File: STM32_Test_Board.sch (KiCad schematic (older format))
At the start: 7 parts, among them J1 Conn_01x16_Male, J2 Conn_01x16_Male, J3 Conn_01x16_Male, J4 Conn_01x16_Male, U1 STM32G484RET6

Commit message: Adding PCB design
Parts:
- U1: footprint LQFP64-10x10mm -> Package_QFP:LQFP-64_10x10mm_P0.5mm
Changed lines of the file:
@@
 F 0 "U1" H 5050 2537 60  0000 C CNN
 F 1 "STM32G484RET6" H 5050 2431 60  0000 C CNN
-F 2 "LQFP64-10x10mm" H 5050 2390 60  0001 C CNN
+F 2 "Package_QFP:LQFP-64_10x10mm_P0.5mm" H 5050 2390 60  0001 C CNN
 F 3 "" H 3650 2150 60  0000 C CNN
 	1    3650 2150
@@
 F 0 "U1" H 9650 3737 60  0000 C CNN
 F 1 "STM32G484RET6" H 9650 3631 60  0000 C CNN
-F 2 "LQFP64-10x10mm" H 10250 3590 60  0001 C CNN
+F 2 "Package_QFP:LQFP-64_10x10mm_P0.5mm" H 10250 3590 60  0001 C CNN
 F 3 "" H 8850 3350 60  0000 C CNN
 	2    8850 3350

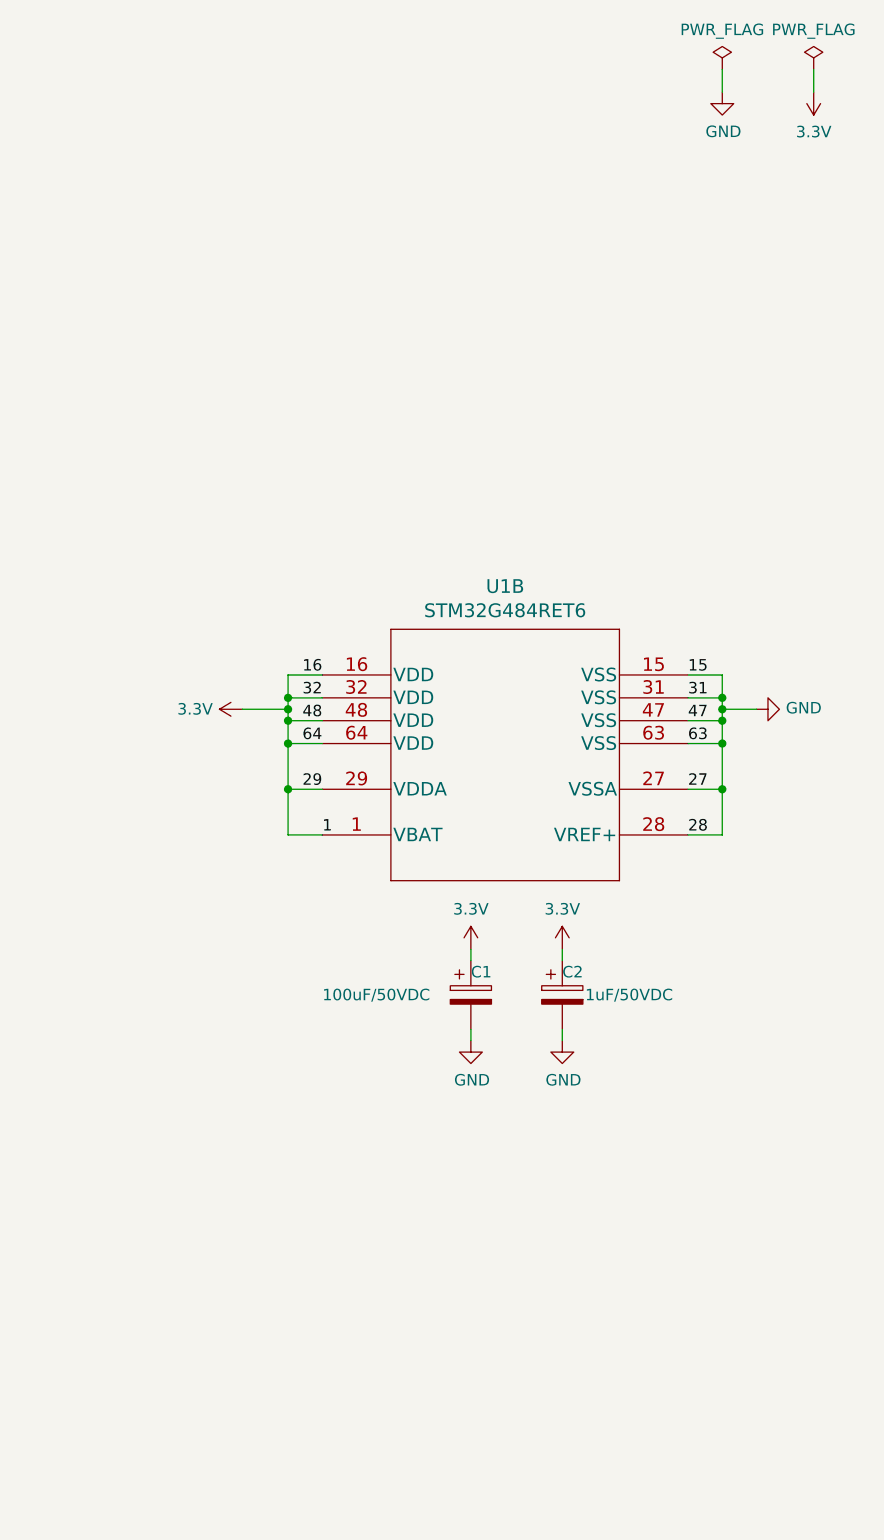
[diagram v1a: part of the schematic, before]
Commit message: Adding decoupling capacitor
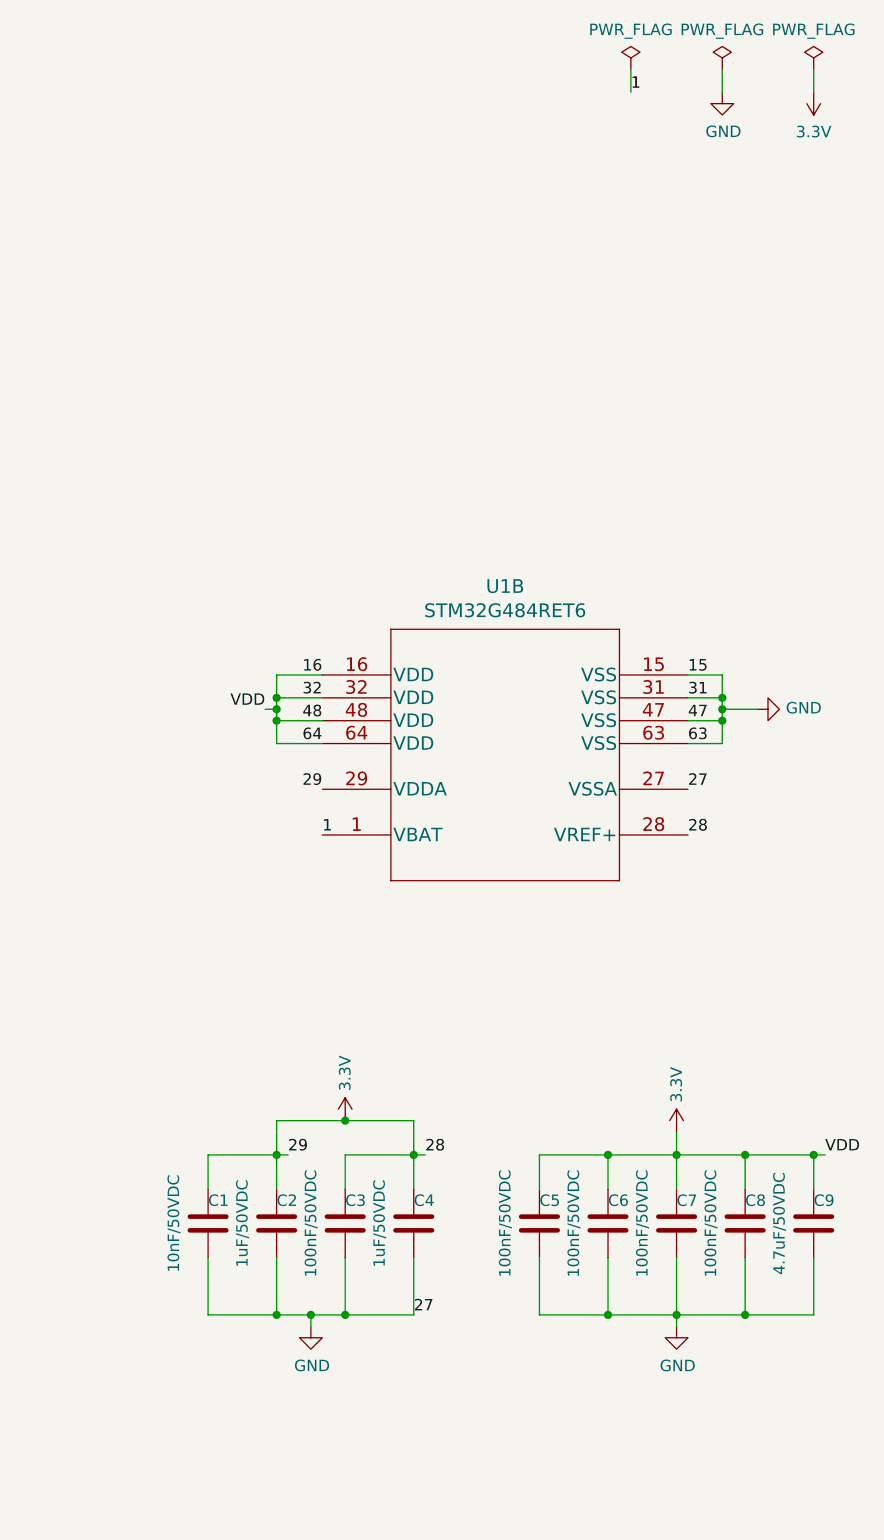
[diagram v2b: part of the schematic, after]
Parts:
- removed C1: 100uF/50VDC, Capacitor_SMD:CP_Elec_5x5.4, symbol Device:CP
- removed C2: 1uF/50VDC, Capacitor_SMD:CP_Elec_5x5.4, symbol Device:CP
- added C1: 10nF/50VDC, Capacitor_SMD:C_0805_2012Metric_Pad1.15x1.40mm_HandSolder, symbol Device:C
- added C2, C4: 1uF/50VDC, Capacitor_SMD:C_0805_2012Metric_Pad1.15x1.40mm_HandSolder, symbol Device:C
- added C3, C5, C6, C7, C8: 100nF/50VDC, Capacitor_SMD:C_0805_2012Metric_Pad1.15x1.40mm_HandSolder, symbol Device:C
- added C9: 4.7uF/50VDC, Capacitor_SMD:C_0805_2012Metric_Pad1.15x1.40mm_HandSolder, symbol Device:C
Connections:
- net 3.3V: now also J2.12 (Pin_12), U1.28 (VREF+), C1.1, C2.1, C3.1, C4.1, C5.1, C6.1, C7.1, C8.1, C9.1; no longer J1.1 (Pin_1), U1.1 (VBAT)
- net GND: now also C1.2, C2.2, C3.2, C4.2, C5.2, C6.2, C7.2, C8.2, C9.2; no longer J2.12 (Pin_12), U1.28 (VREF+)
- new net 1: J1.1 (Pin_1), U1.1 (VBAT)
